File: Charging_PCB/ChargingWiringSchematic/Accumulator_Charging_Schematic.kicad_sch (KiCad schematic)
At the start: 12 parts, among them J1 Amphenol (HVIL), J2 2pin (+/-12V), J3 Conn_01x07_Pin, J4 Conn_01x05_Pin, J5 4pinCharger, J6 12PinDesutcheConn, J7 Charging_PCB, J8 2pin Charger HV, K1 AIR-, K2 AIR+, SW1 ChgShtdwnButton

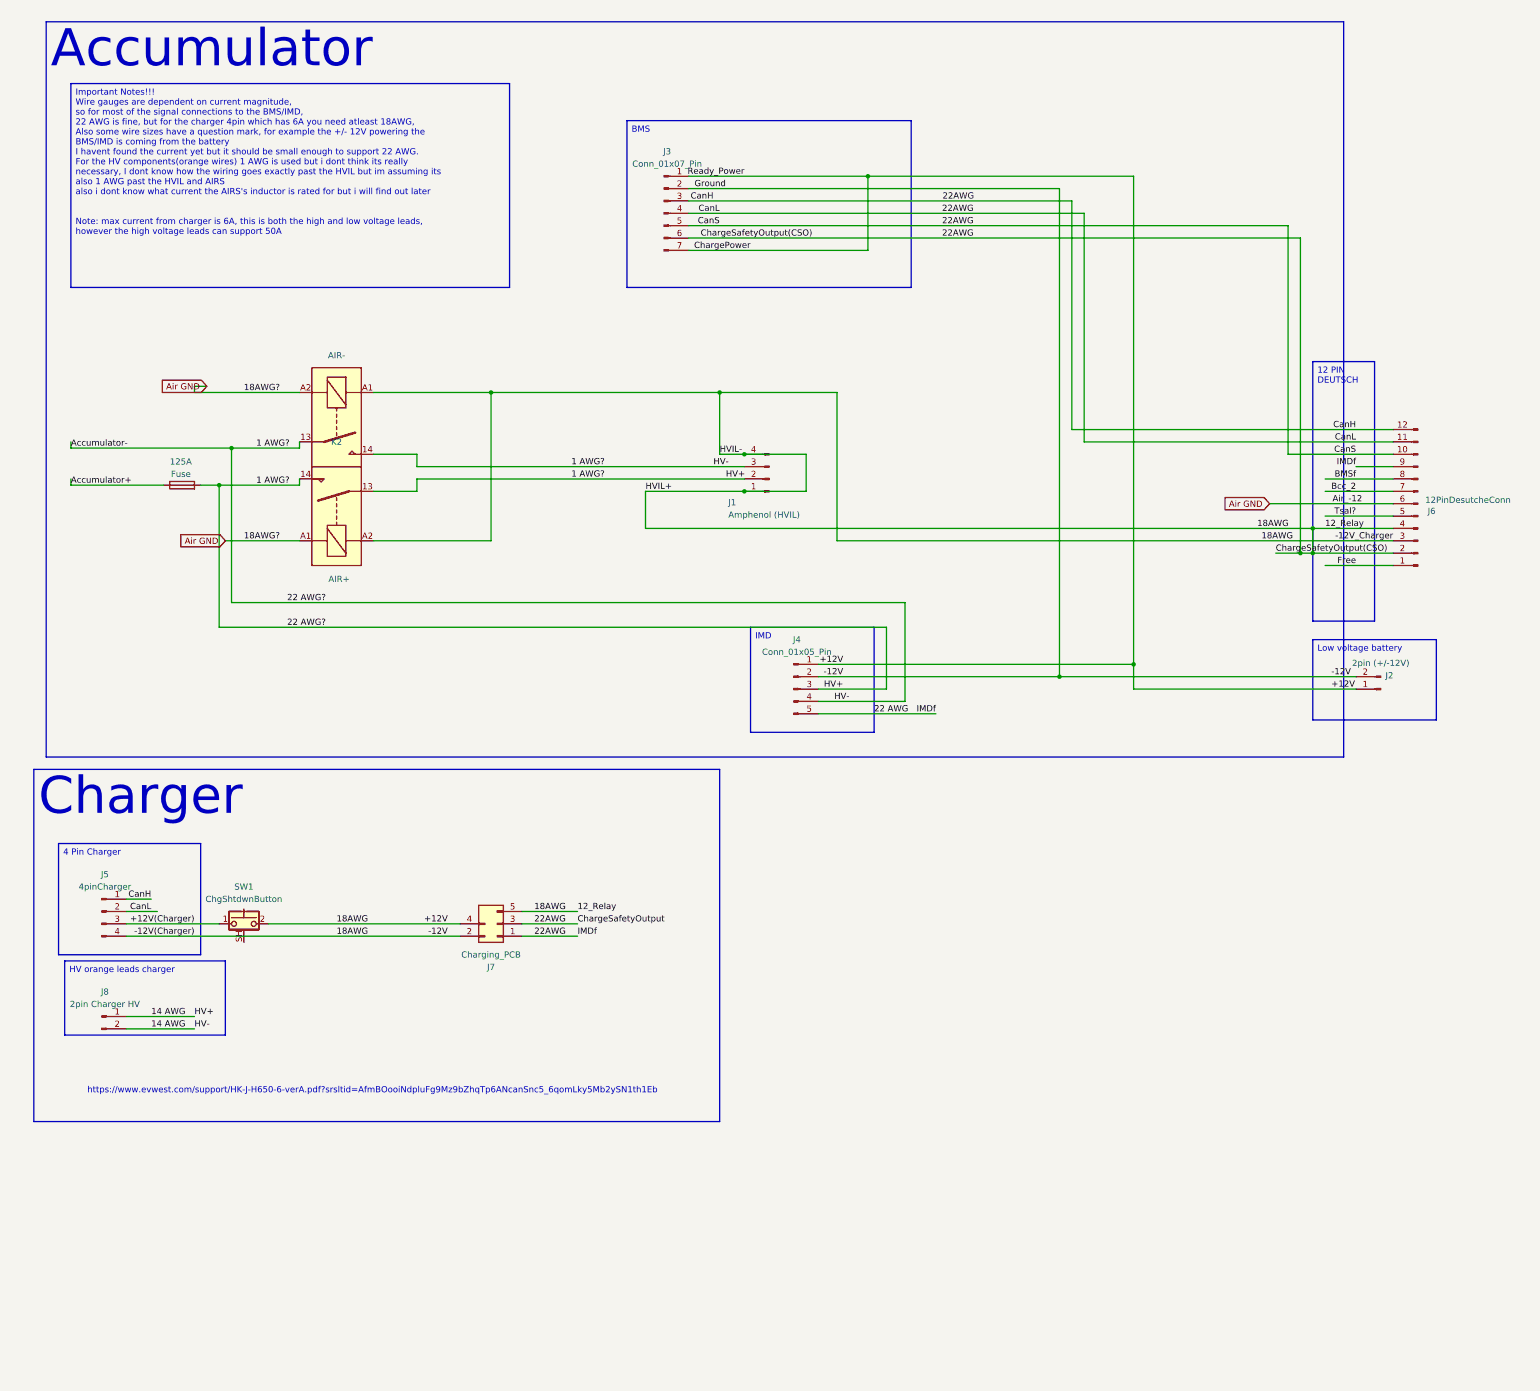
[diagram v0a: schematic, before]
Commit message: ESF documentation and wiring schematics for charging
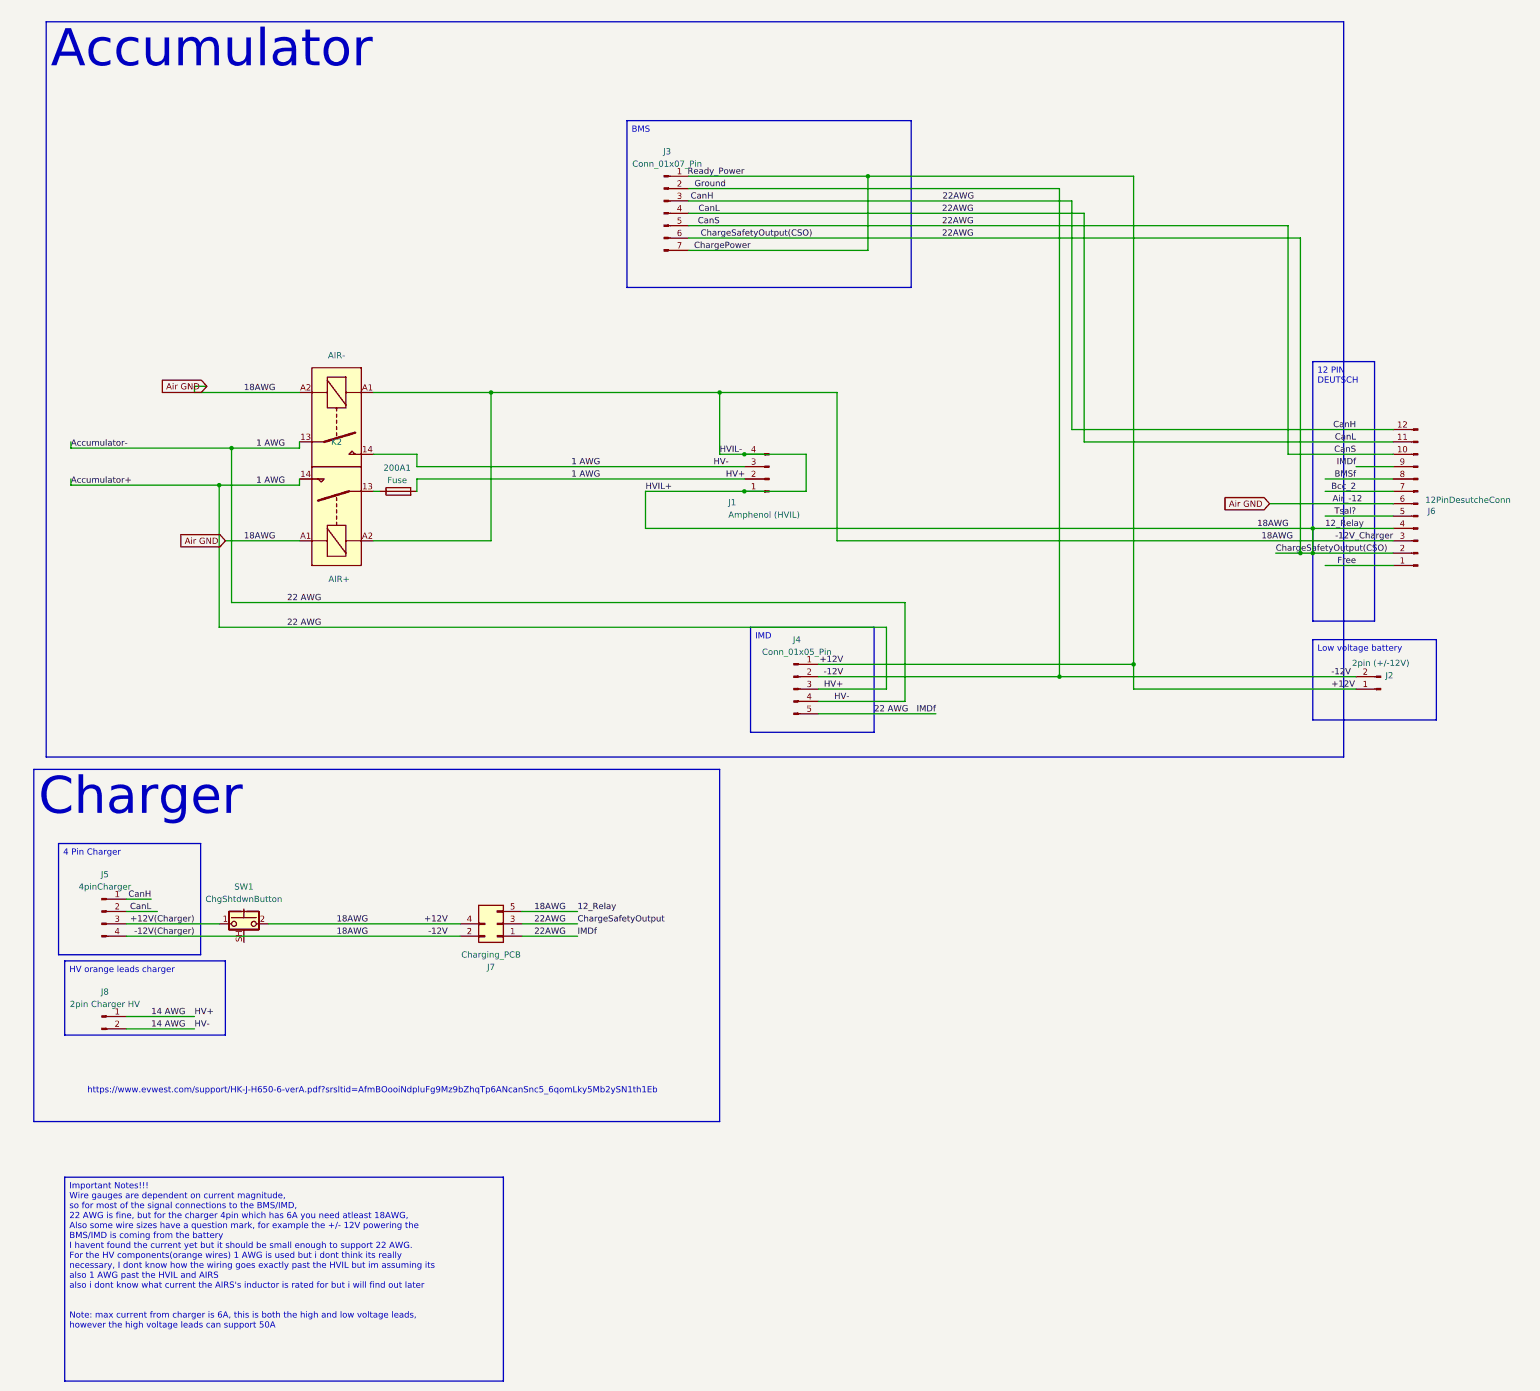
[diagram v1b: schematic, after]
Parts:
- removed 125A: Fuse, symbol Device:Fuse
- added 200A1: Fuse, symbol Device:Fuse
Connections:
- net +12V is gone; now on net Air GND: J1.1 (Pin_1), J1.4 (Pin_4), J2.1 (Pin_1), J2.2 (Pin_2), J3.1 (Pin_1), J3.2 (Pin_2), J3.3 (Pin_3), J3.4 (Pin_4), J3.5 (Pin_5), J3.6 (Pin_6), J3.7 (Pin_7), J4.1 (Pin_1), J4.2 (Pin_2), J4.5 (Pin_5), J5.1 (Pin_1), J5.2 (Pin_2), J5.4 (Pin_4), J6.10 (Pin_10), J6.11 (Pin_11), J6.12 (Pin_12), J6.2 (Pin_2), J6.3 (Pin_3), J6.4 (Pin_4), J6.9 (Pin_9), J7.1 (Pin_1), J7.2 (Pin_2), J7.3 (Pin_3), J7.4 (Pin_4), J7.5 (Pin_5), K1.A1, K2.A2, SW1.2
- net Air GND: now also J1.2 (Pin_2), J1.3 (Pin_3), J4.3 (Pin_3), J4.4 (Pin_4), J8.1 (Pin_1), J8.2 (Pin_2), K1.13, K1.14, K2.14, 200A1.2
- removed net 1 AWG?: J1.2 (Pin_2), J1.3 (Pin_3), J4.3 (Pin_3), J4.4 (Pin_4), J8.1 (Pin_1), J8.2 (Pin_2), K1.13, K1.14, K2.13, K2.14
- new net: 200A1.1, K2.13
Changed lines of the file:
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@@
 	(generator "eeschema")
 	(generator_version "9.0")
-	(paper "A3")
+	(paper "A2")
 	(text "https://www.evwest.com/support/HK-J-H650-6-verA.pdf?srsltid=AfmBOooiNdpluFg9Mz9bZhqTp6ANcanSnc5_6qomLky5Mb2ySN1th1Eb"
 		(exclude_from_sim no)
@@
 	(text_box "Important Notes!!!\nWire gauges are dependent on current magnitude,\nso for most of the signal connections to the BMS/IMD,\n22 AWG is fine, but for the charger 4pin which has 6A you need atleast 18AWG,\nAlso some wire sizes have a question mark, for example the +/- 12V powering the BMS/IMD is coming from the battery\nI havent found the current yet but it should be small enough to support 22 AWG.\nFor the HV components(orange wires) 1 AWG is used but i dont think its really necessary, I dont know how the wiring goes exactly past the HVIL but im assuming its also 1 AWG past the HVIL and AIRS\nalso i dont know what current the AIRS's inductor is rated for but i will find out later\n\n\nNote: max current from charger is 6A, this is both the high and low voltage leads, however the high voltage leads can support 50A"
 		(exclude_from_sim no)
-		(at 20.32 29.21 0)
+		(at 19.05 254 0)
 		(size 90.17 41.91)
 		(margins 0.9525 0.9525 0.9525 0.9525)
@@
 	(wire
 		(pts
-			(xy 46.99 111.76) (xy 50.8 111.76)
-		)
-		(stroke
-			(width 0)
-			(type default)
-		)
-	)
-	(wire
-		(pts
 			(xy 223.52 151.13) (xy 284.48 151.13)
 		)
@@
 	(wire
 		(pts
+			(xy 187.96 140.97) (xy 187.96 153.67)
+		)
+		(stroke
+			(width 0)
+			(type default)
+		)
+	)
+	(wire
+		(pts
+			(xy 106.68 92.71) (xy 106.68 123.19)
+		)
+		(stroke
+			(width 0)
+			(type default)
+		)
+	)
+	(wire
+		(pts
+			(xy 82.55 92.71) (xy 106.68 92.71)
+		)
+		(stroke
+			(width 0)
+			(type default)
+		)
+	)
+	(wire
+		(pts
+			(xy 177.8 123.19) (xy 292.1 123.19)
+		)
+		(stroke
+			(width 0)
+			(type default)
+		)
+	)
+	(wire
+		(pts
+			(xy 228.6 102.87) (xy 292.1 102.87)
+		)
+		(stroke
+			(width 0)
+			(type default)
+		)
+	)
+	(wire
+		(pts
+			(xy 31.75 201.93) (xy 50.8 201.93)
+		)
+		(stroke
+			(width 0)
+			(type default)
+		)
+	)
+	(wire
+		(pts
+			(xy 238.76 153.67) (xy 284.48 153.67)
+		)
+		(stroke
+			(width 0)
+			(type default)
+		)
+	)
+	(wire
+		(pts
+			(xy 278.13 128.27) (xy 292.1 128.27)
+		)
+		(stroke
+			(width 0)
+			(type default)
+		)
+	)
+	(wire
+		(pts
+			(xy 238.76 148.59) (xy 238.76 153.67)
+		)
+		(stroke
+			(width 0)
+			(type default)
+		)
+	)
+	(wire
+		(pts
 			(xy 20.32 111.76) (xy 20.32 110.49)
 		)
@@
 	(wire
 		(pts
-			(xy 187.96 140.97) (xy 187.96 153.67)
-		)
-		(stroke
-			(width 0)
-			(type default)
-		)
-	)
-	(wire
-		(pts
-			(xy 106.68 92.71) (xy 106.68 123.19)
-		)
-		(stroke
-			(width 0)
-			(type default)
-		)
-	)
-	(wire
-		(pts
-			(xy 82.55 92.71) (xy 106.68 92.71)
-		)
-		(stroke
-			(width 0)
-			(type default)
-		)
-	)
-	(wire
-		(pts
-			(xy 177.8 123.19) (xy 292.1 123.19)
-		)
-		(stroke
-			(width 0)
-			(type default)
-		)
-	)
-	(wire
-		(pts
-			(xy 228.6 102.87) (xy 292.1 102.87)
-		)
-		(stroke
-			(width 0)
-			(type default)
-		)
-	)
-	(wire
-		(pts
-			(xy 31.75 201.93) (xy 50.8 201.93)
-		)
-		(stroke
-			(width 0)
-			(type default)
-		)
-	)
-	(wire
-		(pts
-			(xy 238.76 153.67) (xy 284.48 153.67)
-		)
-		(stroke
-			(width 0)
-			(type default)
-		)
-	)
-	(wire
-		(pts
-			(xy 278.13 128.27) (xy 292.1 128.27)
-		)
-		(stroke
-			(width 0)
-			(type default)
-		)
-	)
-	(wire
-		(pts
-			(xy 238.76 148.59) (xy 238.76 153.67)
-		)
-		(stroke
-			(width 0)
-			(type default)
-		)
-	)
-	(wire
-		(pts
 			(xy 138.43 113.03) (xy 158.75 113.03)
 		)
@@
 	(wire
 		(pts
-			(xy 82.55 113.03) (xy 91.44 113.03)
-		)
-		(stroke
-			(width 0)
-			(type default)
-		)
-	)
-	(wire
-		(pts
-			(xy 20.32 111.76) (xy 39.37 111.76)
+			(xy 82.55 113.03) (xy 83.82 113.03)
+		)
+		(stroke
+			(width 0)
+			(type default)
+		)
+	)
+	(wire
+		(pts
+			(xy 20.32 111.76) (xy 50.8 111.76)
 		)
 		(stroke
@@
 		)
 	)
-	(label "22 AWG?"
+	(label "22 AWG"
 		(at 64.77 135.89 0)
 		(effects
@@
 		)
 	)
-	(label "1 AWG?"
+	(label "1 AWG"
 		(at 123.19 110.49 0)
 		(effects
@@
 		)
 	)
-	(label "18AWG?"
+	(label "18AWG"
 		(at 55.88 92.71 0)
 		(effects
@@
 		)
 	)
-	(label "18AWG?"
+	(label "18AWG"
 		(at 55.88 123.19 0)
 		(effects
@@
 		)
 	)
-	(label "1 AWG?"
+	(label "1 AWG"
 		(at 58.42 111.76 0)
 		(effects
@@
 		)
 	)
-	(label "1 AWG?"
+	(label "1 AWG"
 		(at 123.19 107.95 0)
 		(effects
@@
 		)
 	)
-	(label "22 AWG?"
+	(label "22 AWG"
 		(at 64.77 140.97 0)
 		(effects
@@
 		)
 	)
-	(label "1 AWG?"
+	(label "1 AWG"
 		(at 58.42 104.14 0)
 		(effects
@@
 	)
 	(symbol
-		(lib_id "Device:Fuse")
-		(at 43.18 111.76 90)
-		(unit 1)
-		(exclude_from_sim no)
-		(in_bom yes)
-		(on_board yes)
-		(dnp no)
-		(property "Reference" "125A"
-			(at 42.926 106.934 90)
-			(effects
-				(font
-					(size 1.27 1.27)
-				)
-			)
-		)
-		(property "Value" "Fuse"
-			(at 42.926 109.474 90)
-			(effects
-				(font
-					(size 1.27 1.27)
-				)
-			)
-		)
-		(property "Footprint" ""
-			(at 43.18 113.538 90)
-			(effects
-				(font
-					(size 1.27 1.27)
-				)
-				(hide yes)
-			)
-		)
-		(property "Datasheet" "~"
-			(at 43.18 111.76 0)
-			(effects
-				(font
-					(size 1.27 1.27)
-				)
-				(hide yes)
-			)
-		)
-		(property "Description" "Fuse"
-			(at 43.18 111.76 0)
-			(effects
-				(font
-					(size 1.27 1.27)
-				)
-				(hide yes)
-			)
-		)
-		(pin "1"
-		)
-		(pin "2"
-		)
-		(instances
-			(project ""
-				(path "/6f922d61-c977-42d6-8550-7b21896d7733"
-					(reference "125A")
-					(unit 1)
-				)
-			)
-		)
-	)
-	(symbol
 		(lib_id "Connector_Generic:Conn_2Rows-05Pins")
 		(at 107.95 201.93 180)
@@
 					(unit 1)
 				)
+			)
+		)
+	)
+	(symbol
+		(lib_id "Device:Fuse")
+		(at 87.63 113.03 90)
+		(unit 1)
+		(exclude_from_sim no)
+		(in_bom yes)
+		(on_board yes)
+		(dnp no)
+		(property "Reference" "200A1"
+			(at 87.376 108.204 90)
+			(effects
+				(font
+					(size 1.27 1.27)
+				)
+			)
+		)
+		(property "Value" "Fuse"
+			(at 87.376 110.744 90)
+			(effects
+				(font
+					(size 1.27 1.27)
+				)
+			)
+		)
+		(property "Footprint" ""
+			(at 87.63 114.808 90)
+			(effects
+				(font
+					(size 1.27 1.27)
+				)
+				(hide yes)
+			)
+		)
+		(property "Datasheet" "~"
+			(at 87.63 113.03 0)
+			(effects
+				(font
+					(size 1.27 1.27)
+				)
+				(hide yes)
+			)
+		)
+		(property "Description" "Fuse"
+			(at 87.63 113.03 0)
+			(effects
+				(font
+					(size 1.27 1.27)
+				)
+				(hide yes)
+			)
+		)
+		(pin "1"
+		)
+		(pin "2"
+		)
+		(instances
+			(project "Accumulator_Charging_Schematic"
+				(path "/6f922d61-c977-42d6-8550-7b21896d7733"
+					(reference "200A1")
+					(unit 1)
+				)
